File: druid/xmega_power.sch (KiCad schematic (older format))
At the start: 30 parts, among them U4 XC6206P332MR

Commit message: Add some packages
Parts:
- removed W?: BAT_CHARGE_1, Measurement_Points:Test_Point_2Pads, symbol TEST
- removed W?: BAT_CHARGE_2, Measurement_Points:Test_Point_2Pads, symbol TEST
- added W?: TEST_BAT_1_CHARGE, Measurement_Points:Measurement_Point_Square-TH_Small, symbol TEST_1P
- added W?: TEST_BAT_2_CHARGE, Measurement_Points:Measurement_Point_Square-TH_Small, symbol TEST_1P
- W?: value BAT_1 -> TEST_BAT_1
- W?: value BAT2 -> TEST_BAT2
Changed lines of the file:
@@
 	2150 1450 2650 1450
 Wire Wire Line
-	2650 1450 2650 2050
+	2650 1325 2650 2050
 Connection ~ 2650 2050
 Text Label 3325 3000 3    60   ~ 0
-GND
-Text Label 3050 1450 0    60   ~ 0
 GND
 $Comp
@@
 	2150 4650 2650 4650
 Wire Wire Line
-	2650 4650 2650 5250
+	2650 4525 2650 5250
 Connection ~ 2650 5250
 Text Label 3325 6200 3    60   ~ 0
-GND
-Text Label 3050 4650 0    60   ~ 0
 GND
 $Comp
@@
 P 4975 2450
 F 0 "W?" H 4975 2510 50  0000 C CNN
-F 1 "BAT_1" H 4975 2380 50  0000 C CNN
+F 1 "TEST_BAT_1" H 4975 2380 50  0000 C CNN
 F 2 "Measurement_Points:Test_Point_2Pads" H 5225 2600 50  0000 C CNN
 F 3 "" H 4975 2450 50  0000 C CNN
@@
 P 4975 5650
 F 0 "W?" H 4975 5710 50  0000 C CNN
-F 1 "BAT2" H 4975 5580 50  0000 C CNN
+F 1 "TEST_BAT2" H 4975 5580 50  0000 C CNN
 F 2 "Measurement_Points:Test_Point_2Pads" H 5275 5800 50  0000 C CNN
 F 3 "" H 4975 5650 50  0000 C CNN
@@
 $EndComp
 $Comp
-L TEST W?
-U 1 1 5C6BB1A8
-P 2850 1450
-F 0 "W?" H 2850 1510 50  0000 C CNN
-F 1 "BAT_CHARGE_1" H 2875 1575 50  0000 C CNN
-F 2 "Measurement_Points:Test_Point_2Pads" H 3125 1650 50  0000 C CNN
-F 3 "" H 2850 1450 50  0000 C CNN
-	1    2850 1450
-	1    0    0    -1
-$EndComp
-$Comp
-L TEST W?
-U 1 1 5C6BB612
-P 2850 4650
-F 0 "W?" H 2850 4710 50  0000 C CNN
-F 1 "BAT_CHARGE_2" H 2875 4775 50  0000 C CNN
-F 2 "Measurement_Points:Test_Point_2Pads" H 3100 4850 50  0000 C CNN
-F 3 "" H 2850 4650 50  0000 C CNN
-	1    2850 4650
-	1    0    0    -1
-$EndComp
+L TEST_1P W?
+U 1 1 5C6C9437
+P 2650 1325
+F 0 "W?" H 2650 1595 50  0000 C CNN
+F 1 "TEST_BAT_1_CHARGE" H 2650 1525 50  0000 C CNN
+F 2 "Measurement_Points:Measurement_Point_Square-TH_Small" H 2700 1675 50  0000 C CNN
+F 3 "" H 2850 1325 50  0000 C CNN
+	1    2650 1325
+	1    0    0    -1
+$EndComp
+Connection ~ 2650 1450
+$Comp
+L TEST_1P W?
+U 1 1 5C6C9C6E
+P 2650 4525
+F 0 "W?" H 2650 4795 50  0000 C CNN
+F 1 "TEST_BAT_2_CHARGE" H 2650 4725 50  0000 C CNN
+F 2 "Measurement_Points:Measurement_Point_Square-TH_Small" H 2700 4875 50  0000 C CNN
+F 3 "" H 2850 4525 50  0000 C CNN
+	1    2650 4525
+	1    0    0    -1
+$EndComp
+Connection ~ 2650 4650
 $EndSCHEMATC

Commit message: Add packages for LEDs
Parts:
- removed D?: red, symbol LED-RESCUE-xmobile
- removed D?: green, symbol LED-RESCUE-xmobile
- added D?: green, LEDs:LED_0402, symbol LED-RESCUE-xmobile
- added D?: red, LEDs:LED_0402, symbol LED-RESCUE-xmobile
- D? (x2): footprint (none) -> LEDs:LED_0402; case (none) -> 0402 In; example (none) -> https://ru.mouser.com/ProductDetail/ROHM-Semiconductor/SML-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
- W? (x2): symbol TEST -> TEST-RESCUE-xmobile; case (none) -> 2 pads
- W? (x2): case (none) -> 1 pad
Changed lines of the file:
@@
 Text Label 5175 2450 0    60   ~ 0
 GND
-Text Notes 5100 2600 0    60   ~ 0
+Text Notes 5175 2625 0    60   ~ 0
 BAT-
-Text Notes 4850 2600 2    60   ~ 0
+Text Notes 4800 2625 2    60   ~ 0
 BAT+\n
 $Comp
@@
 F 0 "D?" H 2325 2400 50  0000 C CNN
 F 1 "red" H 2325 2200 50  0000 C CNN
-F 2 "" H 2325 2300 50  0001 C CNN
-F 3 "" H 2325 2300 50  0001 C CNN
+F 2 "LEDs:LED_0402" H 2325 2300 50  0001 C CNN
+F 3 "https://ru.mouser.com/datasheet/2/348/sml-p1-e-1139198.pdf" H 2325 2300 50  0001 C CNN
+F 4 "https://ru.mouser.com/ProductDetail/ROHM-Semiconductor/SML-P12U2TT86R?qs=sGAEpiMZZMuCm2JlHBGefsrOrFaWoqzNOGPWK3jFzCB54s8pBFBg3g%3d%3d" H 2325 2300 60  0001 C CNN "example"
+F 5 "0402 In" H 2175 2400 30  0000 C CNN "case"
 	1    2325 2300
 	0    -1   -1   0
@@
 F 0 "D?" H 2025 2400 50  0000 C CNN
 F 1 "green" H 2025 2200 50  0000 C CNN
-F 2 "" H 2025 2300 50  0001 C CNN
-F 3 "" H 2025 2300 50  0001 C CNN
+F 2 "LEDs:LED_0402" H 2025 2300 50  0001 C CNN
+F 3 "https://ru.mouser.com/datasheet/2/348/sml-p1-e-1139198.pdf" H 2025 2300 50  0001 C CNN
+F 4 "https://ru.mouser.com/ProductDetail/ROHM-Semiconductor/SML-P12M2TT86R?qs=sGAEpiMZZMuCm2JlHBGefsrOrFaWoqzNWFfaRj%2fRvVAAroms6JXrzA%3d%3d" H 2025 2300 60  0001 C CNN "example"
+F 5 "0402 In" H 1875 2400 30  0000 C CNN "case"
 	1    2025 2300
 	0    -1   -1   0
@@
 Text Label 5175 5650 0    60   ~ 0
 GND
-Text Notes 5100 5800 0    60   ~ 0
+Text Notes 5175 5825 0    60   ~ 0
 BAT-
-Text Notes 4875 5800 2    60   ~ 0
+Text Notes 4825 5825 2    60   ~ 0
 BAT+\n
-$Comp
-L LED-RESCUE-xmobile D?
-U 1 1 5C6B0922
-P 2325 5500
-F 0 "D?" H 2325 5600 50  0000 C CNN
-F 1 "red" H 2325 5400 50  0000 C CNN
-F 2 "" H 2325 5500 50  0001 C CNN
-F 3 "" H 2325 5500 50  0001 C CNN
-	1    2325 5500
-	0    -1   -1   0
-$EndComp
-$Comp
-L LED-RESCUE-xmobile D?
-U 1 1 5C6B0928
-P 2025 5500
-F 0 "D?" H 2025 5600 50  0000 C CNN
-F 1 "green" H 2025 5400 50  0000 C CNN
-F 2 "" H 2025 5500 50  0001 C CNN
-F 3 "" H 2025 5500 50  0001 C CNN
-	1    2025 5500
-	0    -1   -1   0
-$EndComp
 $Comp
 L R R?
@@
 $EndComp
 $Comp
-L TEST W?
+L TEST-RESCUE-xmobile W?
 U 1 1 5C6B9CD1
 P 4975 2450
+AR Path="/5C6B9CD1" Ref="W?"  Part="1"
+AR Path="/5A9FCB78/5C6B9CD1" Ref="W?"  Part="1"
 F 0 "W?" H 4975 2510 50  0000 C CNN
 F 1 "TEST_BAT_1" H 4975 2380 50  0000 C CNN
-F 2 "Measurement_Points:Test_Point_2Pads" H 5225 2600 50  0000 C CNN
+F 2 "Measurement_Points:Test_Point_2Pads" H 5225 2600 50  0001 C CNN
 F 3 "" H 4975 2450 50  0000 C CNN
+F 4 "2 pads" H 4975 2575 30  0000 C CNN "case"
 	1    4975 2450
 	1    0    0    -1
 $EndComp
 $Comp
-L TEST W?
+L TEST-RESCUE-xmobile W?
 U 1 1 5C6BA4AE
 P 4975 5650
+AR Path="/5C6BA4AE" Ref="W?"  Part="1"
+AR Path="/5A9FCB78/5C6BA4AE" Ref="W?"  Part="1"
 F 0 "W?" H 4975 5710 50  0000 C CNN
 F 1 "TEST_BAT2" H 4975 5580 50  0000 C CNN
-F 2 "Measurement_Points:Test_Point_2Pads" H 5275 5800 50  0000 C CNN
+F 2 "Measurement_Points:Test_Point_2Pads" H 5275 5800 50  0001 C CNN
 F 3 "" H 4975 5650 50  0000 C CNN
+F 4 "2 pads" H 4975 5775 30  0000 C CNN "case"
 	1    4975 5650
 	1    0    0    -1
@@
 F 0 "W?" H 2650 1595 50  0000 C CNN
 F 1 "TEST_BAT_1_CHARGE" H 2650 1525 50  0000 C CNN
-F 2 "Measurement_Points:Measurement_Point_Square-TH_Small" H 2700 1675 50  0000 C CNN
+F 2 "Measurement_Points:Measurement_Point_Square-TH_Small" H 2700 1675 50  0001 C CNN
 F 3 "" H 2850 1325 50  0000 C CNN
+F 4 "1 pad" H 2775 1450 30  0000 C CNN "case"
 	1    2650 1325
 	1    0    0    -1
@@
 F 0 "W?" H 2650 4795 50  0000 C CNN
 F 1 "TEST_BAT_2_CHARGE" H 2650 4725 50  0000 C CNN
-F 2 "Measurement_Points:Measurement_Point_Square-TH_Small" H 2700 4875 50  0000 C CNN
+F 2 "Measurement_Points:Measurement_Point_Square-TH_Small" H 2700 4875 50  0001 C CNN
 F 3 "" H 2850 4525 50  0000 C CNN
+F 4 "1 pad" H 2800 4650 30  0000 C CNN "case"
 	1    2650 4525
 	1    0    0    -1
 $EndComp
 Connection ~ 2650 4650
+$Comp
+L LED-RESCUE-xmobile D?
+U 1 1 5C6CA596
+P 2025 5500
+F 0 "D?" H 2025 5600 50  0000 C CNN
+F 1 "green" H 2025 5400 50  0000 C CNN
+F 2 "LEDs:LED_0402" H 2025 5500 50  0001 C CNN
+F 3 "https://ru.mouser.com/datasheet/2/348/sml-p1-e-1139198.pdf" H 2025 5500 50  0001 C CNN
+F 4 "https://ru.mouser.com/ProductDetail/ROHM-Semiconductor/SML-P12M2TT86R?qs=sGAEpiMZZMuCm2JlHBGefsrOrFaWoqzNWFfaRj%2fRvVAAroms6JXrzA%3d%3d" H 2025 5500 60  0001 C CNN "example"
+F 5 "0402 In" H 1875 5600 30  0000 C CNN "case"
+	1    2025 5500
+	0    -1   -1   0
+$EndComp
+$Comp
+L LED-RESCUE-xmobile D?
+U 1 1 5C6CB16E
+P 2325 5500
+F 0 "D?" H 2325 5600 50  0000 C CNN
+F 1 "red" H 2325 5400 50  0000 C CNN
+F 2 "LEDs:LED_0402" H 2325 5500 50  0001 C CNN
+F 3 "https://ru.mouser.com/datasheet/2/348/sml-p1-e-1139198.pdf" H 2325 5500 50  0001 C CNN
+F 4 "https://ru.mouser.com/ProductDetail/ROHM-Semiconductor/SML-P12U2TT86R?qs=sGAEpiMZZMuCm2JlHBGefsrOrFaWoqzNOGPWK3jFzCB54s8pBFBg3g%3d%3d" H 2325 5500 60  0001 C CNN "example"
+F 5 "0402 In" H 2175 5600 30  0000 C CNN "case"
+	1    2325 5500
+	0    -1   -1   0
+$EndComp
 $EndSCHEMATC

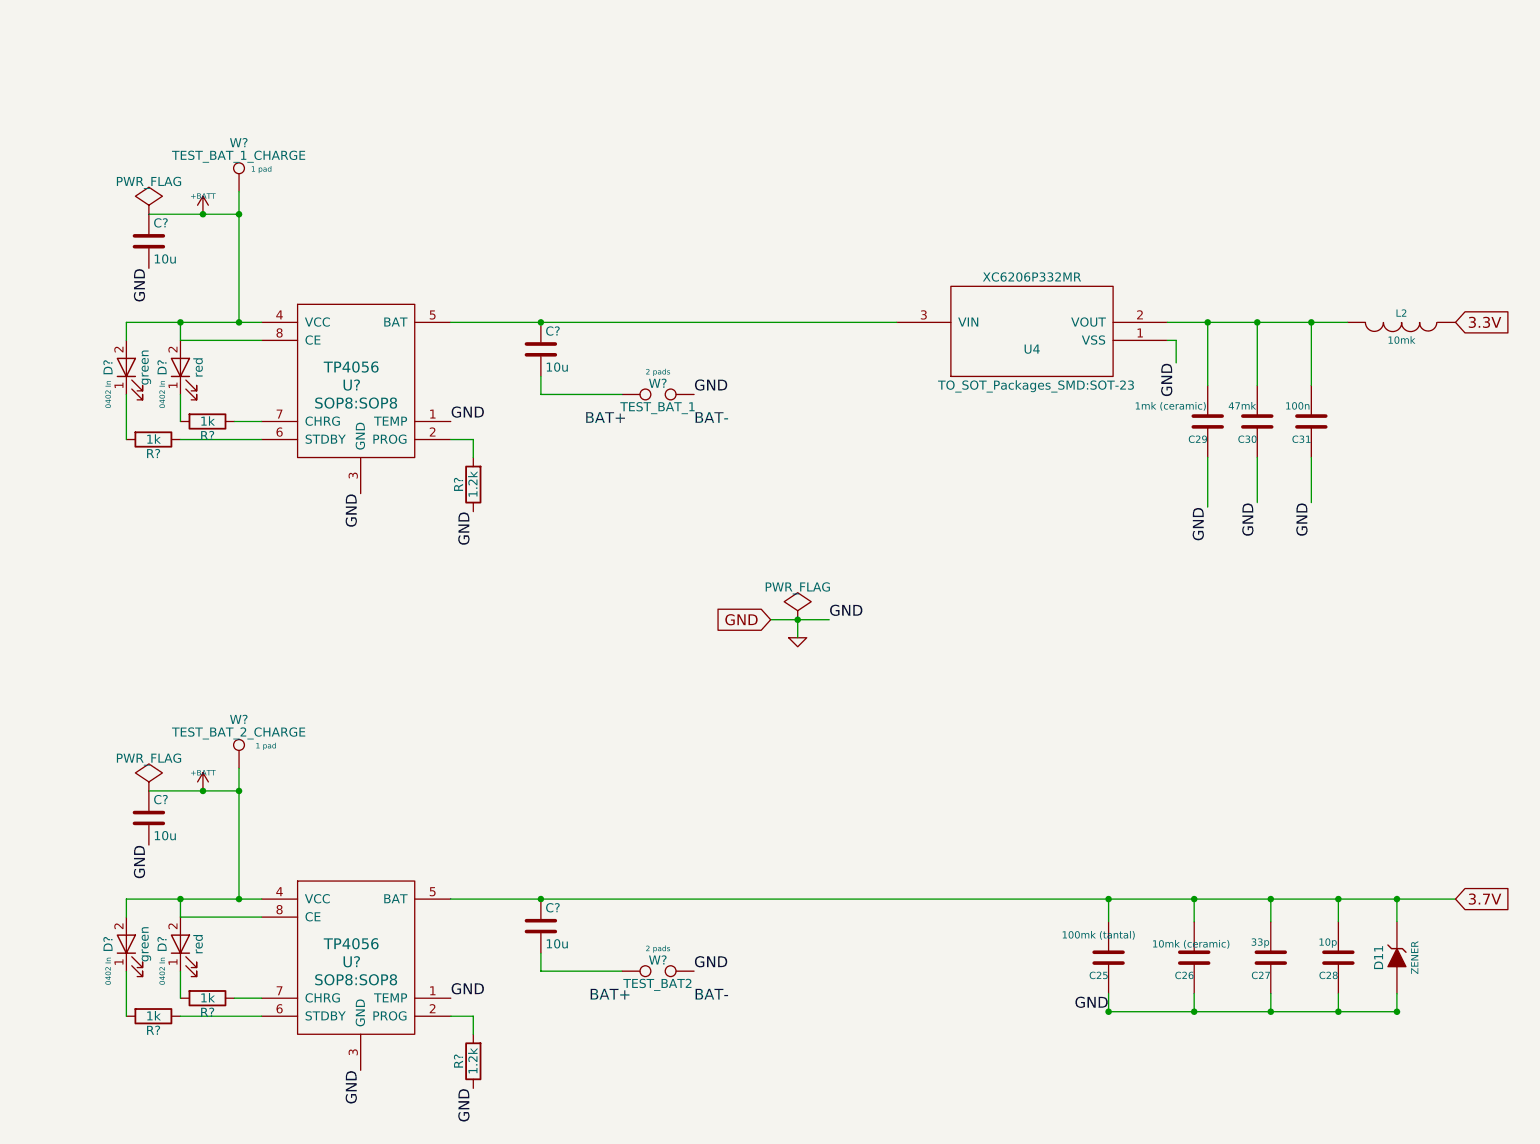
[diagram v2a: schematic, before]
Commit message: Added footprints for some elments in power module
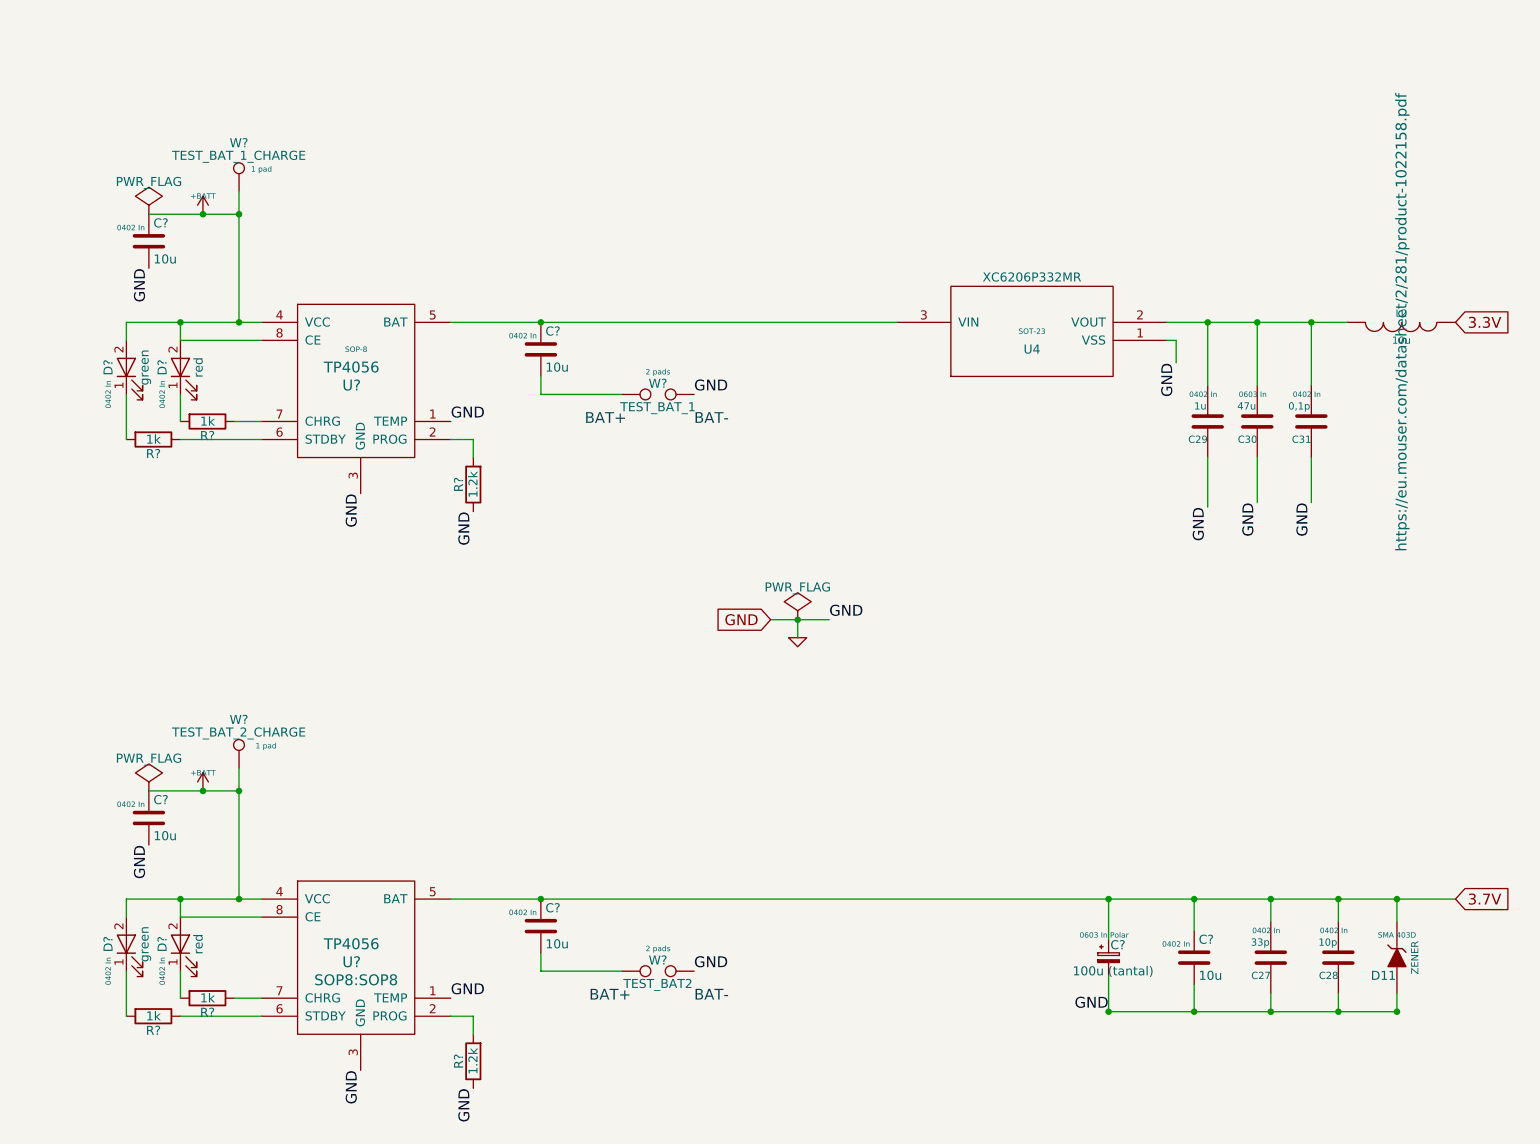
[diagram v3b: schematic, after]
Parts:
- removed C25: 100mk (tantal), symbol C-RESCUE-xmobile
- removed C26: 10mk (ceramic), symbol C-RESCUE-xmobile
- removed C? (x3): 10u, symbol C
- added C? (x4): 10u, Capacitors_SMD:C_0402, symbol C
- added C?: 100u (tantal), 0603_In_tantalum:C_0603, symbol CP_Small
- C27: case (none) -> 0402 In; example (none) -> https://eu.mouser.com/ProductDetail/KEMET/C0402C330J9RACAUT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
- C28: footprint (none) -> Capacitors_SMD:C_0402; case (none) -> 0402 In; example (none) -> https://eu.mouser.com/ProductDetail/AVX/04026A100JAT2A?qs=s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
- C29: value 1mk (ceramic) -> 1u; footprint (none) -> Capacitors_SMD:C_0402; case (none) -> 0402 In; example (none) -> https://eu.mouser.com/ProductDetail/Murata-Electronics/GRM1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
- C30: value 47mk -> 47u; footprint (none) -> Capacitors_SMD:C_0603; case (none) -> 0603 In; example (none) -> https://eu.mouser.com/ProductDetail/Murata-Electronics/ZRB1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
- C31: value 100n -> 0,1p; footprint (none) -> Capacitors_SMD:C_0402; case (none) -> 0402 In; example (none) -> https://eu.mouser.com/ProductDetail/Murata-Electronics/GJM1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
- C?: footprint (none) -> Capacitors_SMD:C_0402; case (none) -> 0402 In; example (none) -> https://eu.mouser.com/ProductDetail/Murata-Electronics/GRM1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
- D11: footprint (none) -> Diodes_SMD:SMA_Standard; case  (none) -> SMA 403D; example (none) -> https://eu.mouser.com/ProductDetail/ON-Semiconductor/1SMA59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
- L2: value 10mk -> 10u; example (none) -> https://eu.mouser.com/ProductDetail/Murata-Electronics/1276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
- U4: case (none) -> SOT-23; example (none) -> https://eu.mouser.com/ProductDetail/Torex-Semiconductor/XC6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
- U?: case (none) -> SOP-8; example (none) -> https://ru.aliexpress.com/item/20-TP4056-TP4056/32965308715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
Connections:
- net +BATT: now also C?.1
- net 3.7V: now also C?.1, C?.1, C?.1
- net GND: now also C?.2, C?.2, C?.2
- net at U4.3 (VIN), U?.5 (BAT): now also C?.1
- net at W?.1: now also C?.2 (x2)
